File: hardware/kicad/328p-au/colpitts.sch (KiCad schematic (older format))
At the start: 25 parts, among them P4 LOOP, Q3 BSS138, Q4 BC817-40, T1 78601/9C

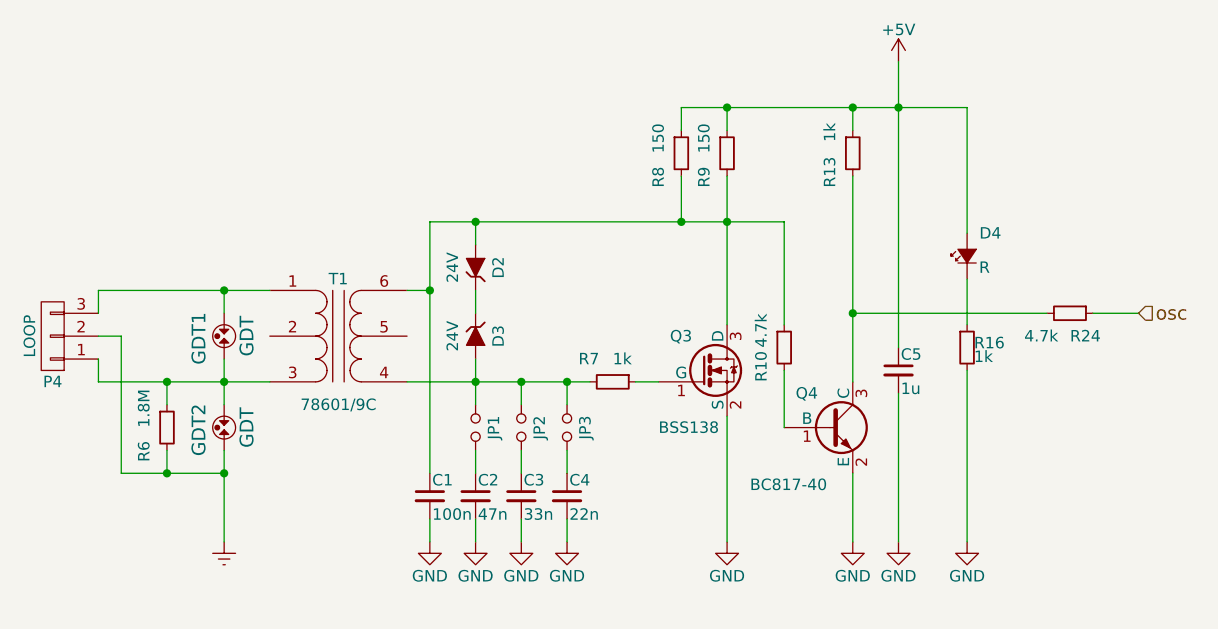
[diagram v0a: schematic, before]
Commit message: hardware/kicad/328p-au: use 3x2 jumper block for frequency selection
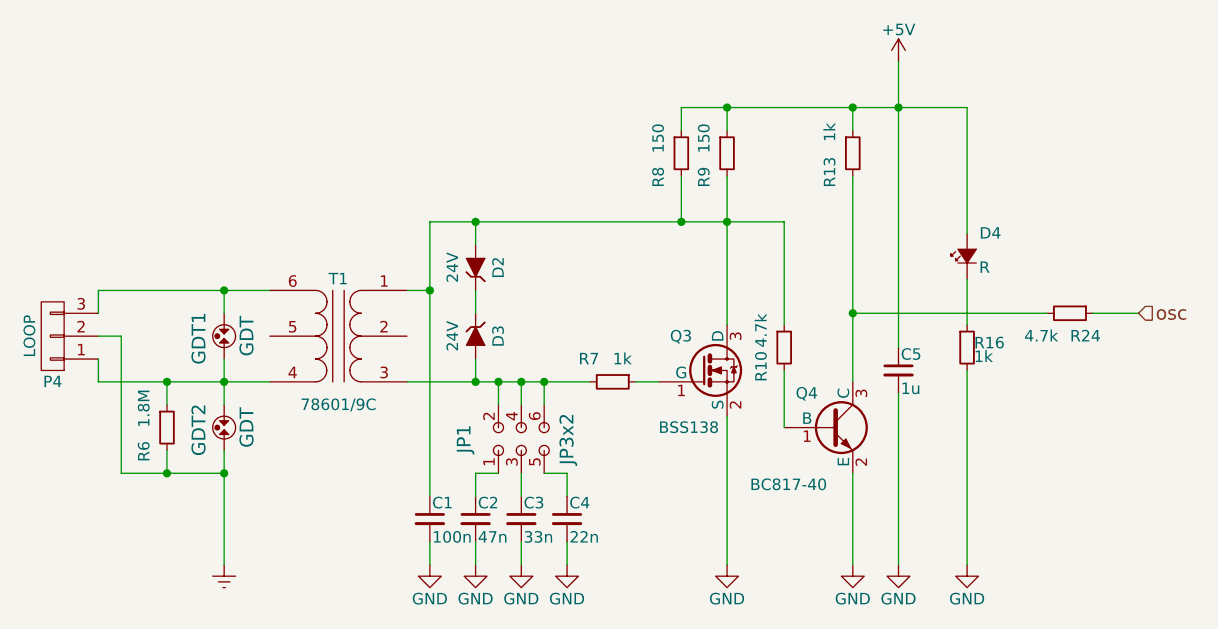
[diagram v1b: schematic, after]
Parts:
- removed JP1, JP2, JP3: Jumper_NO_Small, Pin_Headers:Pin_Header_Straight_1x02, symbol Jumper_NO_Small
- added JP1: JP3x2, Pin_Headers:Pin_Header_Straight_2x03, symbol JP3x2
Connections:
- net at GDT1.1, P4.3 (P3): now also T1.6 (SB); no longer T1.1 (AA)
- net at GDT1.2, GDT2.1, P4.1 (P1)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: now also T1.4 (SA); no longer T1.3 (AB)
- net at D3.2 (A), R7.2: now also T1.3 (AB), JP1.2, JP1.4, JP1.6; no longer T1.4 (SA)
- net at C1.1, D2.2 (A), Q3.3 (D)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: now also T1.1 (AA); no longer T1.6 (SB)
- net at C2.1: now also JP1.1
- net at C3.1: now also JP1.3
- net at C4.1: now also JP1.5
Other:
- moved on the sheet: C1, C2, C3, C4
